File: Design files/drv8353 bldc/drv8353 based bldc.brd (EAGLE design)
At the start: 178 x 122 mm, 126 parts, among them IC1 DRV8353RSRGZT, J3 2X6 FEMALE, J4 B06B-HCMKK

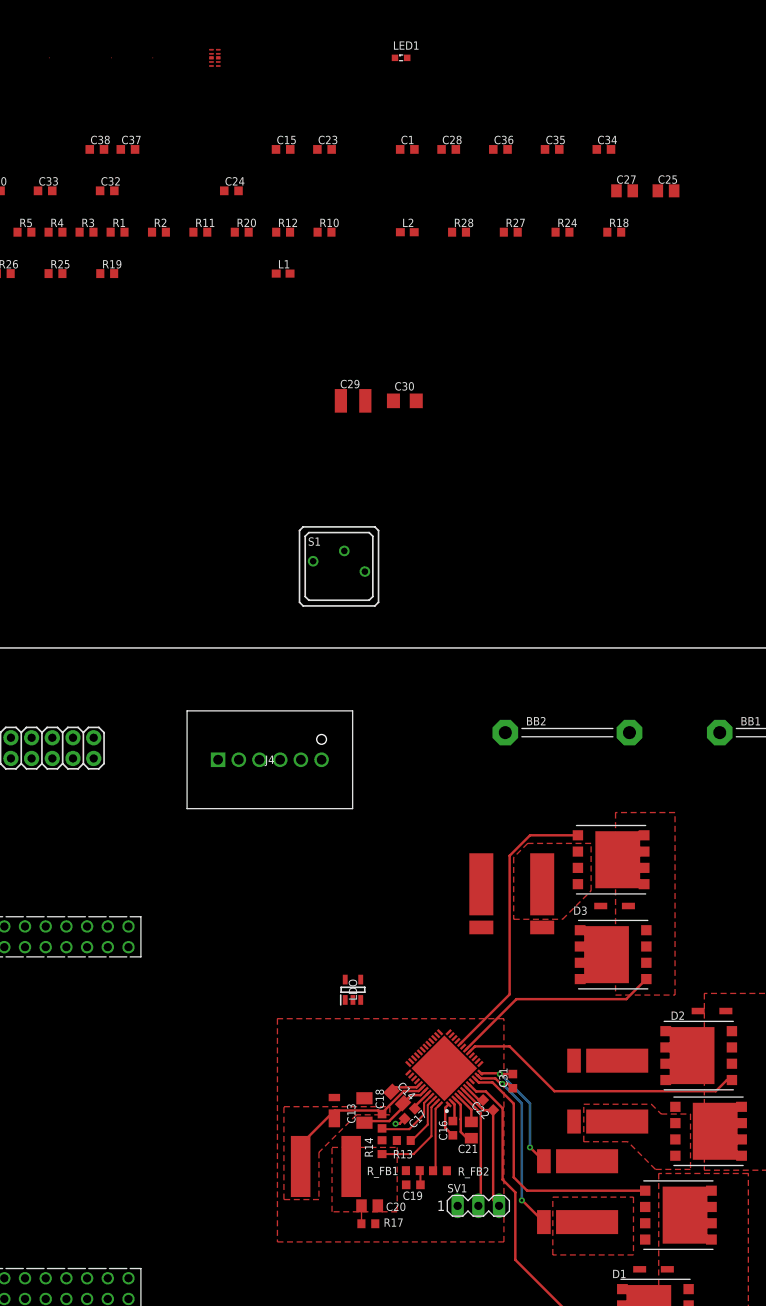
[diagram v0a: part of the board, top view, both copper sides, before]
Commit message: adds layout for Shunt amplifiers on B and C phases (minus capacitor on C)
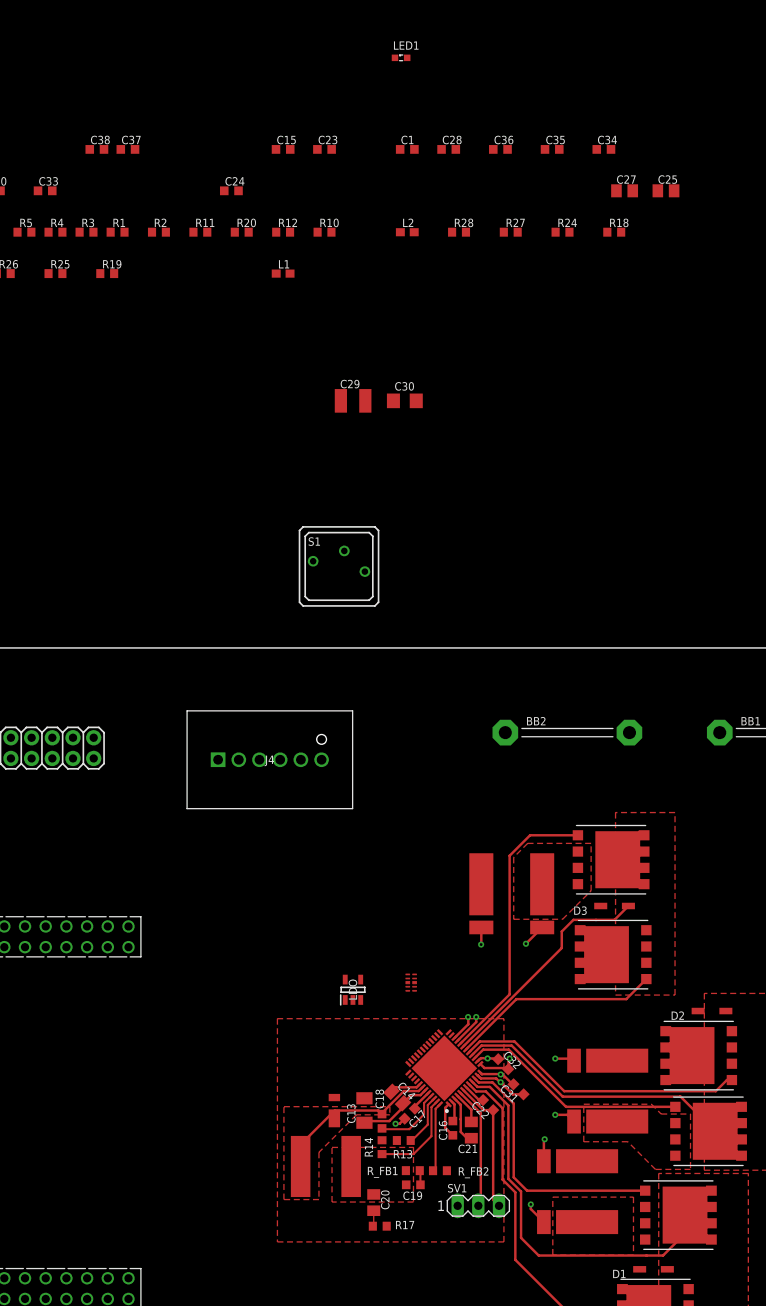
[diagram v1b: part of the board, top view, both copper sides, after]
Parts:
- moved U$25 159.0 mm to (132.1, 31.4)
- moved U$27 145.4 mm to (136.2, 50.9)
- moved U$30 125.3 mm to (125.9, 72.6)
- moved C32 117.7 mm to (114.5, 54.9), turned to 315 degrees
- moved TVS_DIODE 116.0 mm to (103.2, 64.9)
- moved R17 1.43 mm to (99.4, 35.0)
- moved C31 1.22 mm to (116.4, 51.8), turned to 135 degrees
- moved C20 0.64 mm to (98.6, 37.9), turned to 90 degrees
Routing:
- net SHA: track 0.00 -> 38.9 mm
- net SHB: track 0.00 -> 28.7 mm
- net GLB: track 0.00 -> 28.0 mm
- net SHC: track 0.00 -> 23.9 mm
- net SPC: track 0.00 -> 18.2 mm, vias 0 -> 2
- net SPB: track 0.00 -> 16.7 mm, vias 0 -> 2
- net SNC: track 0.00 -> 15.0 mm, vias 0 -> 2
- net SNB: track 0.00 -> 14.6 mm, vias 0 -> 2
- net APHASE: track 0.00 -> 8.11 mm
- net BPHASE: track 0.00 -> 6.09 mm
- net CPHASE: track 0.00 -> 4.68 mm
- net SPA: track 24.1 -> 26.0 mm
- net SNA: track 17.1 -> 17.8 mm

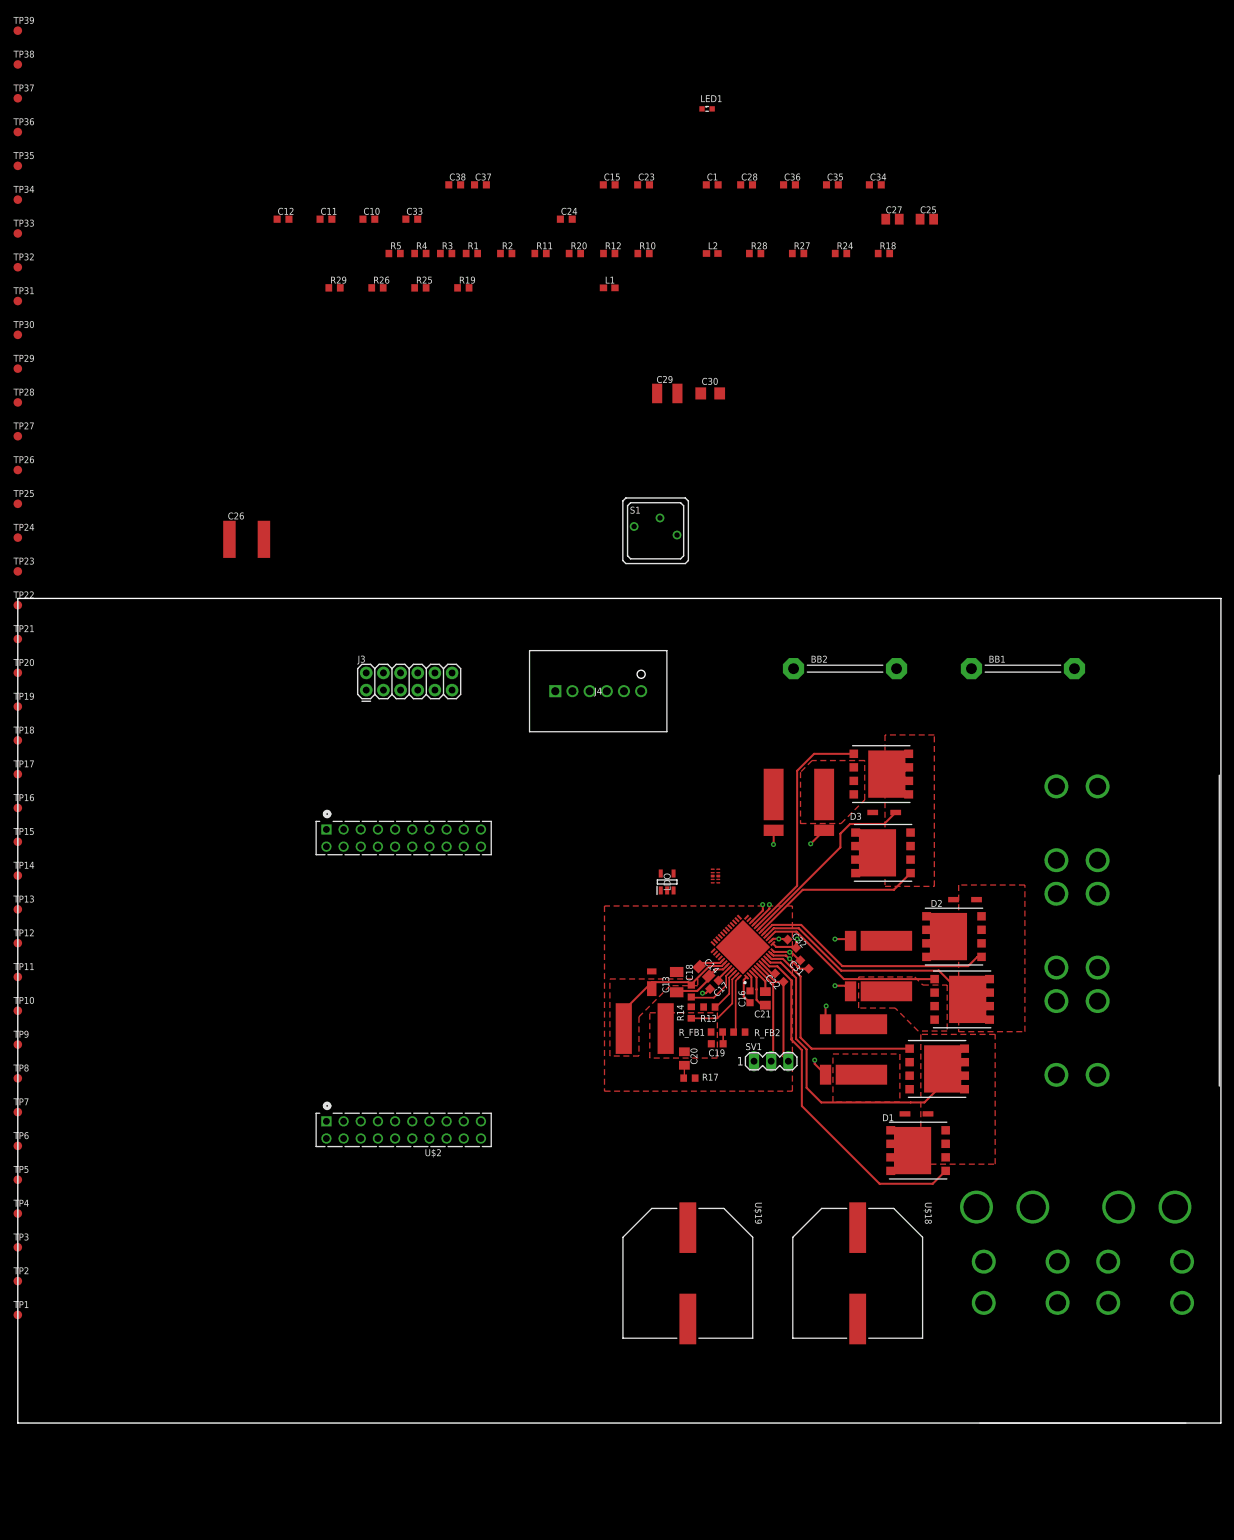
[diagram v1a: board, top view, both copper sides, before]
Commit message: moves fets around
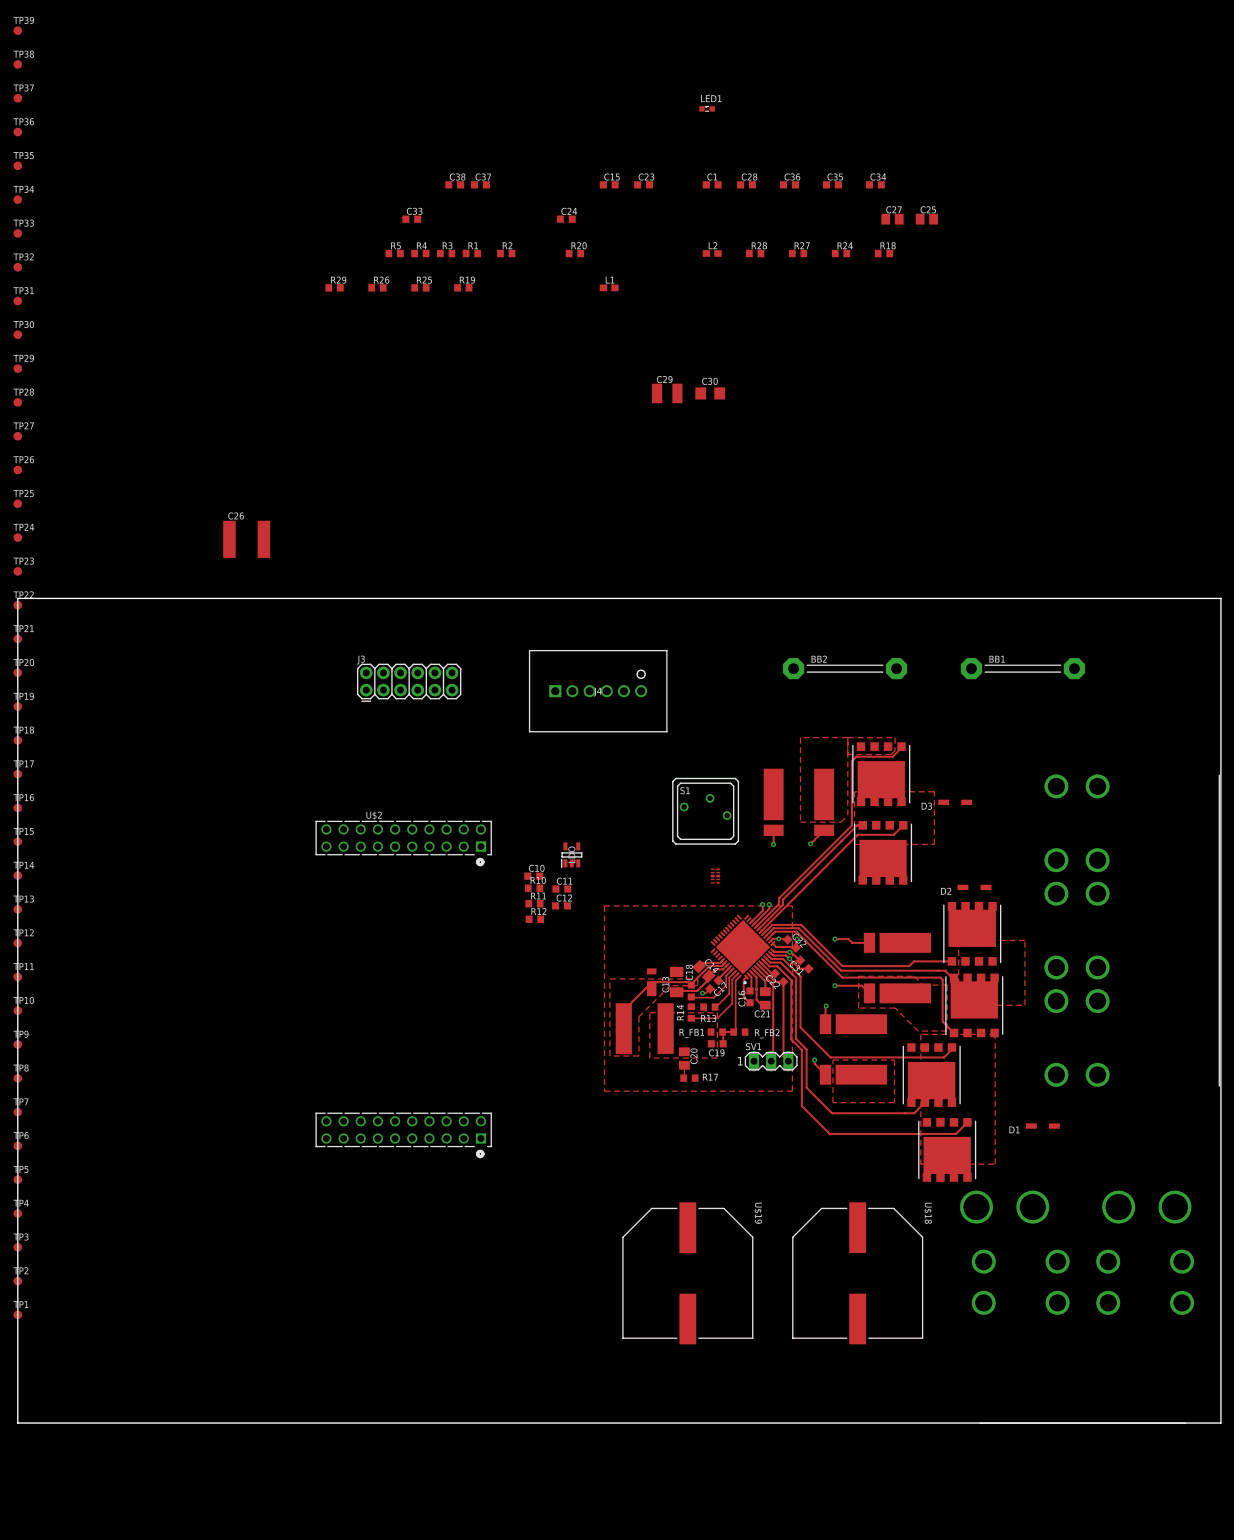
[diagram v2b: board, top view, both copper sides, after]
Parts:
- moved C12 109.6 mm to (80.4, 60.5)
- moved C11 105.1 mm to (80.5, 63.0)
- moved C10 100.2 mm to (76.3, 64.9)
- moved R12 99.1 mm to (76.5, 58.5)
- moved R11 96.2 mm to (76.4, 60.8)
- moved R10 95.3 mm to (76.4, 63.1)
- moved S1 42.2 mm to (101.8, 74.5)
- moved D1 18.8 mm to (151.7, 27.9)
- moved LDO 14.7 mm to (82.0, 68.0)
- moved D3 10.6 mm to (138.7, 75.8)
- moved U$30 4.72 mm to (121.9, 70.1)
- moved U$14 4.30 mm to (137.5, 24.4), turned to 180 degrees
- moved U$4 2.82 mm to (130.2, 51.3)
- moved U$22 2.73 mm to (141.2, 56.4), turned to 0 degrees
- moved D2 2.28 mm to (141.5, 63.2)
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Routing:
- net GLB: track 28.0 -> 37.8 mm
- net GLA: track 31.9 -> 38.7 mm
- net SHC: track 23.9 -> 18.2 mm
- net GHB: track 35.9 -> 31.3 mm
- net GLC: track 35.0 -> 38.7 mm
- net SPB: track 16.7 -> 19.6 mm
- net SNB: track 14.6 -> 17.5 mm
- net GHC: track 25.7 -> 27.6 mm
- net FB: track 10.3 -> 11.9 mm
- net BPHASE: track 6.09 -> 7.22 mm
- net CPHASE: track 4.68 -> 4.06 mm

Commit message: turned thermals off for output connector, added via stiching and planes across all layers
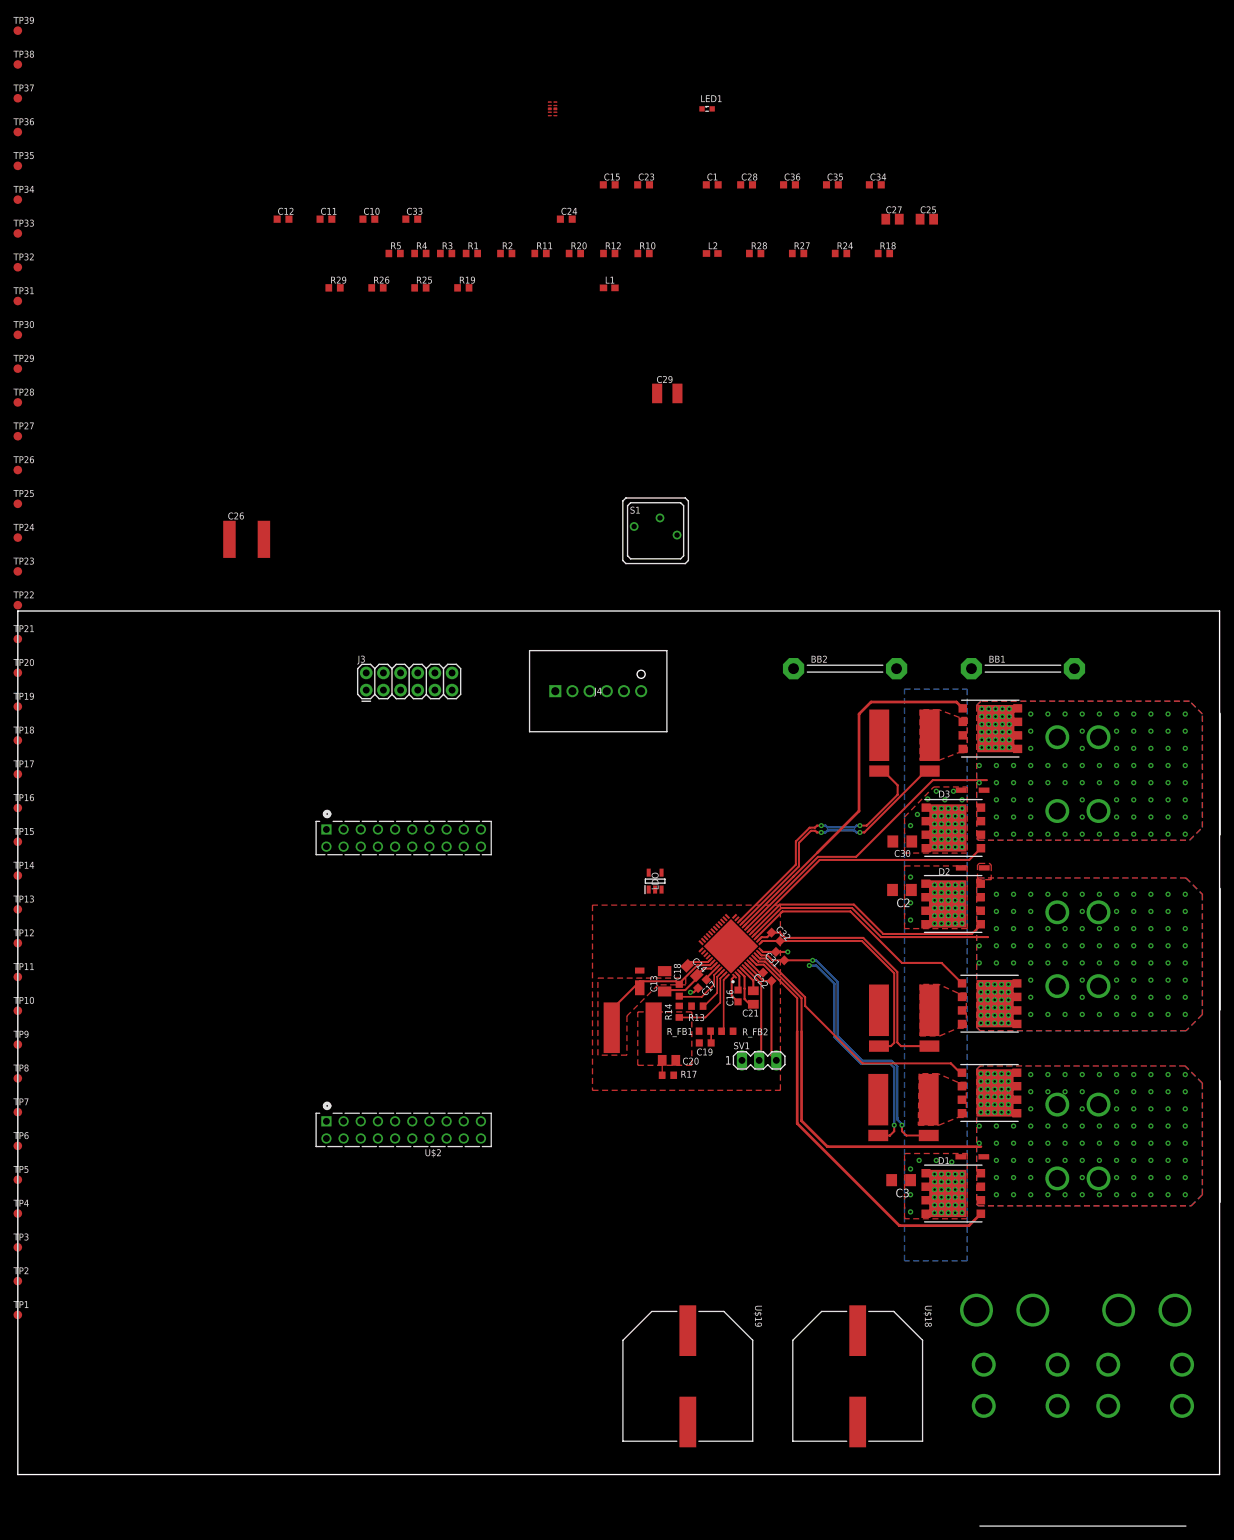
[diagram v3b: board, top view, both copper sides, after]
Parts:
- removed C37, C38: 1uF, rcl:C0603K
- removed U$1: TRIPPLE-MINI-PP75, REV BLDC:TRIPPLE-MINI-PP75
- removed U$25, U$27, U$30: NET_TIE, REV BLDC:CNT
- added C2, C3: 1uF, rcl:C1206
- added U$6, U$7, U$8: MINI-PP75, REV BLDC:MINI-PP75
- D1, D2, D3: device semicon-smd-ipc:SOD123 -> REV BLDC:SOD123
- moved TVS_DIODE 116.0 mm to (79.1, 178.4)
- moved C12 109.6 mm to (39.2, 162.1)
- moved C11 105.1 mm to (45.6, 162.1)
- moved C10 100.2 mm to (51.9, 162.1)
- moved R12 99.1 mm to (87.5, 157.0)
- moved R11 96.2 mm to (77.3, 157.0)
- moved R10 95.3 mm to (92.6, 157.0)
- moved C30 72.1 mm to (130.9, 70.0), turned to 180 degrees
- moved S1 42.2 mm to (94.4, 116.0)
- moved U$5 17.9 mm to (131.2, 84.6)
- moved U$24 17.5 mm to (143.9, 86.7), turned to 270 degrees
- moved U$16 15.2 mm to (157.6, -13.5)
- moved U$18 15.2 mm to (124.3, -9.09)
- moved U$19 15.2 mm to (99.1, -9.09)
- moved F1 15.2 mm to (156.5, 0.71)
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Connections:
- removed net SHA: IC1.9, TP32.TP, U$25.P$2
- removed net SHB: IC1.16, TP6.TP, U$27.P$2
- removed net SHC: IC1.19, TP12.TP, U$30.P$2
- net APHASE: now also IC1.9, TP32.TP, U$8.B1, U$8.B2, U$8.B3, U$8.B4; no longer U$1.A1, U$1.A2, U$1.A3, U$1.A4, U$25.P$1
- net BPHASE: now also IC1.16, TP6.TP, U$7.B1, U$7.B2, U$7.B3, U$7.B4; no longer U$1.B1, U$1.B2, U$1.B3, U$1.B4, U$27.P$1
- net CPHASE: now also IC1.19, TP12.TP, U$6.B1, U$6.B2, U$6.B3, U$6.B4; no longer U$1.C1, U$1.C2, U$1.C3, U$1.C4, U$30.P$1
- net GND: now also C2.2, C3.2; no longer C37.2, C38.2
- net VDRAIN: now also C2.1, C3.1; no longer C37.1, C38.1
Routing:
- net APHASE: track 7.79 -> 55.9 mm, vias 0 -> 115
- net CPHASE: track 4.06 -> 44.7 mm, vias 0 -> 110
- net SHA: track 38.8 -> 0.00 mm
- net BPHASE: track 7.22 -> 38.1 mm, vias 0 -> 113
- net SHB: track 28.7 -> 0.00 mm
- net SNA: track 17.8 -> 43.6 mm, vias 2 -> 3
- net SNC: track 15.0 -> 38.4 mm
- net SPC: track 18.2 -> 39.4 mm
- net SPA: track 26.0 -> 46.3 mm
- net SPB: track 19.6 -> 38.8 mm, vias 2 -> 0
- net SHC: track 18.2 -> 0.00 mm
- net SNB: track 17.5 -> 34.6 mm, vias 2 -> 0
- net GLC: track 38.7 -> 55.3 mm
- net GHC: track 27.6 -> 39.4 mm
- net GHA: track 51.5 -> 62.4 mm
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- added copper zone on layer 15, net APHASE
- added copper zone on layer 16, net APHASE
- added copper zone on layer 2, net APHASE
- added copper zone on layer 15, net BPHASE
- added copper zone on layer 16, net BPHASE
- added copper zone on layer 2, net BPHASE
- added copper zone on layer 15, net CPHASE
- added copper zone on layer 16, net CPHASE
- added copper zone on layer 2, net CPHASE
- added copper zone on layer 1, net VDRAIN
- added copper zone on layer 15, net VDRAIN
- added copper zone on layer 16, net VDRAIN
- added copper zone on layer 2, net VDRAIN
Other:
- board size 178 x 122 mm -> 177.8 x 127.8 mm

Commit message: rerouted current sense signals to layer 15
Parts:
- moved U$3 2.36 mm to (131.0, 33.1), turned to 0 degrees
- moved U$4 2.33 mm to (131.2, 46.2), turned to 0 degrees
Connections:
- net GND: now also U$3.I1, U$4.I1; no longer U$3.I2, U$4.I2
- net N$22: now also U$4.I2; no longer U$4.I1
- net N$24: now also U$3.I2; no longer U$3.I1
- net SNA: now also U$3.E1; no longer U$3.E2
- net SNB: now also U$4.E1; no longer U$4.E2
- net SPA: now also U$3.E2; no longer U$3.E1
- net SPB: now also U$4.E2; no longer U$4.E1
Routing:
- net SNA: track 43.6 -> 28.4 mm, vias 3 -> 2
- net SNB: track 34.6 -> 19.7 mm, vias 0 -> 2
- net SPA: track 46.3 -> 33.8 mm
- net SPB: track 38.8 -> 28.4 mm, vias 0 -> 2
- net SNC: track 38.4 -> 30.8 mm
- net SPC: track 39.4 -> 38.3 mm
- net GLA: track 38.4 -> 39.3 mm
- net GLB: track 37.1 -> 37.8 mm

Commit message: modifies current sense traces for noise immunity
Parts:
- moved C33 112.6 mm to (108.8, 61.5), turned to 135 degrees
- moved C31 0.25 mm to (113.0, 53.1), turned to 90 degrees
- moved C32 0.15 mm to (112.2, 56.1), turned to 270 degrees
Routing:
- net SNB: track 19.7 -> 27.8 mm
- net SNC: track 30.8 -> 38.8 mm
- net SNA: track 28.4 -> 32.7 mm
- net SPC: track 38.3 -> 40.5 mm
- net SPB: track 28.4 -> 29.3 mm
